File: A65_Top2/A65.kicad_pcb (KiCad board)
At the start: 2 copper layers, 314.4 x 98.8 mm, 82 parts, among them J10 Conn_01x01, J11 Conn_01x01, J12 Conn_01x01, J13 Conn_01x01, J14 Conn_01x01, J15 Conn_01x01, J16 Conn_01x01, J17 Conn_01x01, J2 Conn_01x01, J3 Conn_01x01, J4 Conn_01x01, J5 Conn_01x01, J6 Conn_01x01, J7 Conn_01x01, J8 Conn_01x01, J9 Conn_01x01, SW1 SW_PUSH, SW10 SW_PUSH, SW11 SW_PUSH, SW12 SW_PUSH, SW13 SW_PUSH, SW14 SW_PUSH, SW15 SW_PUSH, SW16 SW_PUSH, SW17 SW_PUSH, SW18 SW_PUSH, SW19 SW_PUSH, SW2 KEY_SWITCH, SW20 SW_PUSH, SW21 SW_PUSH, SW22 SW_PUSH, SW23 SW_PUSH, SW24 SW_PUSH, SW25 SW_PUSH, SW26 SW_PUSH, SW27 SW_PUSH, SW28 SW_PUSH, SW29 SW_PUSH, SW3 SW_PUSH, SW30 SW_PUSH, SW31 SW_PUSH, SW32 SW_PUSH, SW33 SW_PUSH, SW34 SW_PUSH, SW35 SW_PUSH, SW36 SW_PUSH, SW37 SW_PUSH, SW38 SW_PUSH, SW39 SW_PUSH, SW4 KEY_SWITCH, SW40 SW_PUSH, SW41 SW_PUSH, SW42 SW_PUSH, SW43 SW_PUSH, SW44 SW_PUSH, SW45 SW_PUSH, SW46 SW_PUSH, SW47 SW_PUSH, SW48 SW_PUSH, SW49 SW_PUSH, SW5 SW_PUSH, SW50 SW_PUSH, SW51 SW_PUSH, SW52 SW_PUSH, SW53 SW_PUSH, SW54 SW_PUSH, SW55 SW_PUSH, SW56 SW_PUSH, SW57 SW_PUSH, SW58 SW_PUSH, SW59 SW_PUSH, SW6 SW_PUSH, SW60 SW_PUSH, SW61 SW_PUSH, SW62 SW_PUSH, SW63 SW_PUSH, SW64 SW_PUSH, SW65 SW_PUSH, SW66 SW_PUSH, SW7 SW_PUSH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

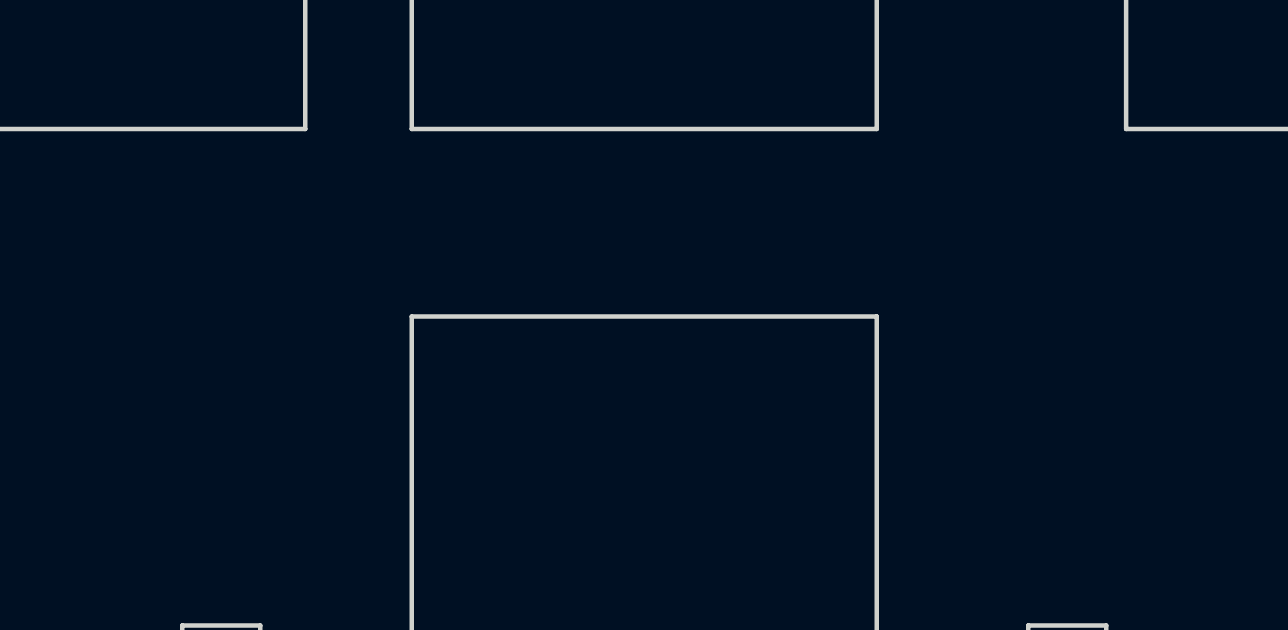
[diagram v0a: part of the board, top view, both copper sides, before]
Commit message: Fixed reset switch position.
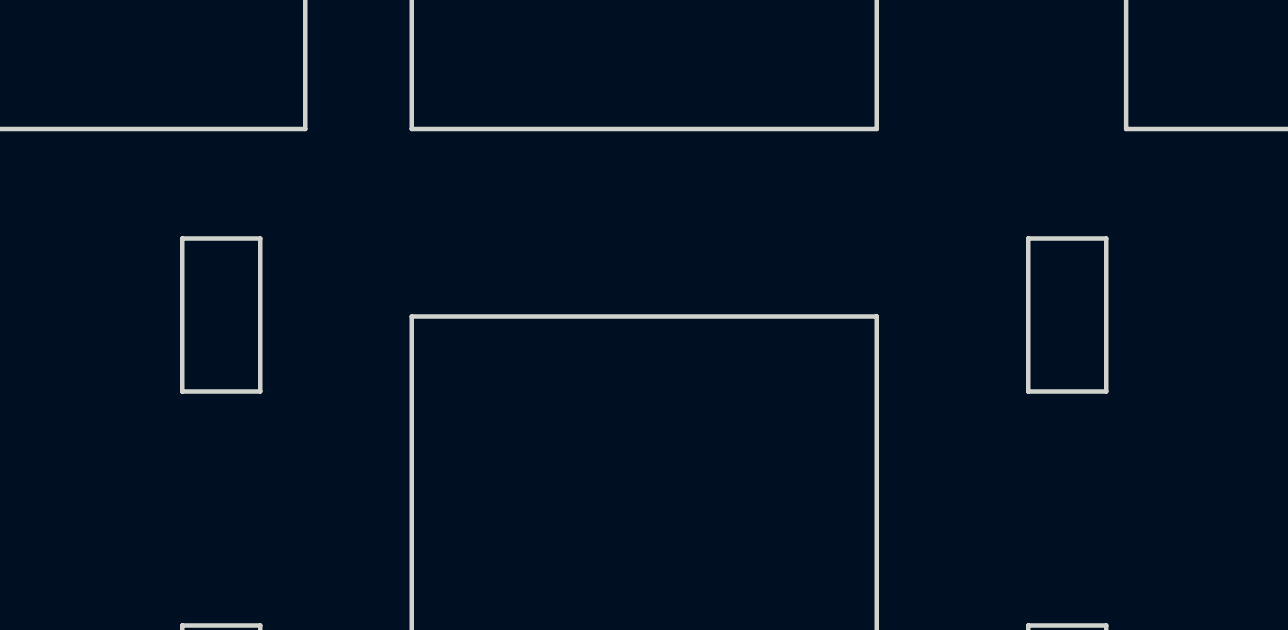
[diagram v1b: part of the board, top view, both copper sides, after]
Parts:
- added SW69: SW_PUSH, new_footprint:SW_Hole_ALPS_2u, F.Cu at (242.9, 104.8)
